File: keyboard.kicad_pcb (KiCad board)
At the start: 2 copper layers, 138.6 x 152.9 mm, 53 parts, among them SW1 SW_PUSH, U1 ATMEGA32U4, X1 XTAL_GND

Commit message: AHHHHHHHHHHHHHHHHHH
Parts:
- removed C1, C2, C3, C4, C5, C6, C7: 22pF, Capacitor_SMD:C_0805_2012Metric_Pad1.15x1.40mm_HandSolder
- removed D_SPACE: D, keyboard_parts:D_SOD123_axial
- removed K_SPACE: KEYSW, MX_Alps_Hybrid:MX-1U-NoLED
- removed R1, R2: 10k, Resistor_SMD:R_0805_2012Metric_Pad1.15x1.40mm_HandSolder
- removed R3, R4: 22, Resistor_SMD:R_0805_2012Metric_Pad1.15x1.40mm_HandSolder
- removed SW1: SW_PUSH, Button_Switch_SMD:SW_SPST_TL3342
- removed USB1: Molex-0548190589, keyboard_parts:Molex-0548190589-Assembly
- removed X1: XTAL_GND, Crystal:Crystal_SMD_5032-4Pin_5.0x3.2mm
- added D_SPACE19: D, keyboard_parts:D_SOD123_axial, F.Cu at (292.9, 131.0)
- added K_SPACE19: KEYSW, MX_Alps_Hybrid:MX-1U-NoLED, F.Cu at (292.9, 126.2)
- U1: value ATMEGA32U4 -> Elite-C-castellated-24pin; footprint Package_QFP:TQFP-44_10x10mm_P0.8mm -> Keebio-Parts:Elite-C-castellated-24pin
- moved K_SPACE10 241.9 mm to (331.0, 173.8)
- moved K_SPACE6 241.9 mm to (254.8, 173.8)
- moved K_SPACE18 239.7 mm to (292.9, 245.3)
- moved K_SPACE4 239.7 mm to (221.5, 150.0)
- moved K_SPACE2 239.7 mm to (254.8, 131.0)
- moved K_SPACE9 239.7 mm to (311.9, 169.1)
- moved K_SPACE1 239.7 mm to (235.7, 131.0)
- moved K_SPACE11 239.7 mm to (221.5, 188.1)
- moved K_SPACE12 239.7 mm to (292.9, 188.1)
- moved K_SPACE13 239.7 mm to (235.7, 207.2)
- moved K_SPACE15 239.7 mm to (273.8, 207.2)
- moved K_SPACE16 239.7 mm to (292.9, 207.2)
- moved K_SPACE17 239.7 mm to (292.9, 226.2)
- moved K_SPACE3 239.7 mm to (273.8, 131.0)
- moved K_SPACE5 239.7 mm to (221.5, 169.1)
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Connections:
- D_SPACE1 pad 1: /row1 -> row0
- D_SPACE10 pad 1: /row3 -> row1
- D_SPACE11 pad 1: /row4 -> row2
- D_SPACE12 pad 1: /row4 -> row2
- D_SPACE13 pad 1: /row5 -> row2
- D_SPACE14 pad 1: /row5 -> row2
- D_SPACE15 pad 1: /row5 -> row2
- D_SPACE16 pad 1: /row5 -> row3
- D_SPACE17 pad 1: /row6 -> row4
- D_SPACE18 pad 1: /row7 -> row5
- D_SPACE2 pad 1: /row1 -> row0
- D_SPACE3 pad 1: /row1 -> row0
- D_SPACE4 pad 1: /row2 -> row0
- D_SPACE5 pad 1: /row3 -> row1
- D_SPACE6 pad 1: /row3 -> row1
- D_SPACE7 pad 1: /row3 -> row1
- D_SPACE8 pad 1: /row3 -> row1
- D_SPACE9 pad 1: /row3 -> row1
- K_SPACE1 pad 1: /col1 -> col1
- K_SPACE10 pad 1: /col6 -> col6
- K_SPACE11 pad 1: /col0 -> col0
- K_SPACE12 pad 1: /col4 -> col4
- K_SPACE13 pad 1: /col1 -> col1
- K_SPACE14 pad 1: /col2 -> col2
- K_SPACE15 pad 1: /col3 -> col3
- K_SPACE16 pad 1: /col4 -> col4
- K_SPACE17 pad 1: /col4 -> col4
- K_SPACE18 pad 1: /col4 -> col4
- K_SPACE2 pad 1: /col2 -> col2
- K_SPACE3 pad 1: /col3 -> col3
- K_SPACE4 pad 1: /col0 -> col0
- K_SPACE5 pad 1: /col0 -> col0
- K_SPACE6 pad 1: /col2 -> col2
- K_SPACE7 pad 1: /col3 -> col3
- K_SPACE8 pad 1: /col4 -> col4
- K_SPACE9 pad 1: /col5 -> col5
- U1 pad 1: Net-(U1-Pad1) -> unconnected-(U1-Pad1)
- U1 pad 10: /row2 -> row5
- U1 pad 11: /row3 -> unconnected-(U1-Pad11)
- U1 pad 12: /row7 -> unconnected-(U1-Pad12)
- U1 pad 13: Net-(R1-Pad1) -> col0
- U1 pad 14: VCC -> col1
- U1 pad 15: GND -> col2
- U1 pad 16: Net-(C1-Pad1) -> col3
- U1 pad 17: Net-(C2-Pad1) -> col4
- U1 pad 18: /col2 -> col5
- U1 pad 19: /col3 -> col6
- U1 pad 2: VCC -> unconnected-(U1-Pad2)
- U1 pad 20: /col4 -> unconnected-(U1-Pad20)
- U1 pad 21: /col5 -> unconnected-(U1-Pad21)
- U1 pad 22: Net-(U1-Pad22) -> unconnected-(U1-Pad22)
- U1 pad 23: GND -> unconnected-(U1-Pad23)
- U1 pad 24: VCC -> unconnected-(U1-Pad24)
- U1 pad 3: Net-(R3-Pad1) -> unconnected-(U1-Pad3)
- U1 pad 4: Net-(R4-Pad1) -> unconnected-(U1-Pad4)
- U1 pad 5: GND -> row0
- U1 pad 6: Net-(C3-Pad1) -> row1
- U1 pad 7: Net-(U1-Pad7) -> row2
- U1 pad 8: /row0 -> row3
- U1 pad 9: /row1 -> row4
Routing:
- net row1: track 0.00 -> 194.1 mm, vias 0 -> 1
- net row2: track 0.00 -> 188.3 mm, vias 0 -> 2
- net row0: track 0.00 -> 145.7 mm, vias 0 -> 2
- net row5: track 0.00 -> 142.5 mm, vias 0 -> 1
- net row4: track 0.00 -> 122.9 mm, vias 0 -> 1
- net col6: track 0.00 -> 108.7 mm
- net col2: track 0.00 -> 102.3 mm
- net col0: track 0.00 -> 102.1 mm
- net col3: track 0.00 -> 91.9 mm
- net col5: track 0.00 -> 88.3 mm
- net col1: track 0.00 -> 39.8 mm
- net col4: track 0.00 -> 31.8 mm, vias 0 -> 1
- net Net-(D_SPACE14-Pad2): track 0.00 -> 9.84 mm
- net Net-(D_SPACE2-Pad2): track 0.00 -> 9.84 mm
- net Net-(D_SPACE13-Pad2): track 0.00 -> 9.84 mm
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- removed copper zone on B.Cu, net GND
- removed copper zone on F.Cu, net VCC
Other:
- board size 138.6 x 152.9 mm -> 131 x 166.7 mm
- net class Default removed

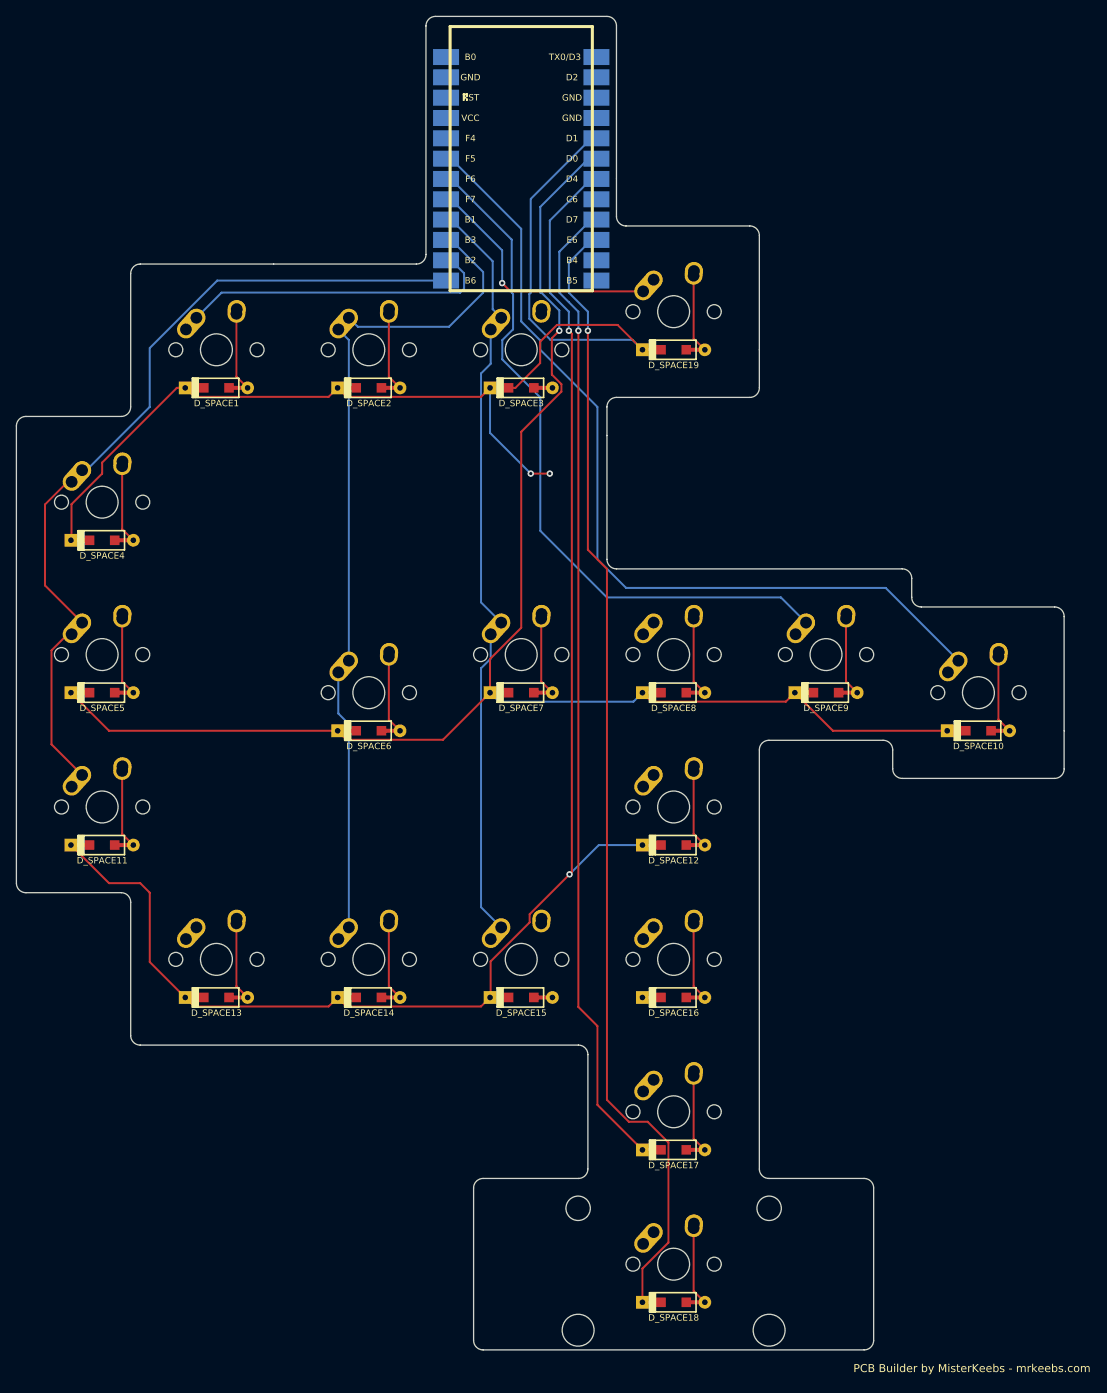
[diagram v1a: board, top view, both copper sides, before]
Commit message: RP2040 rework
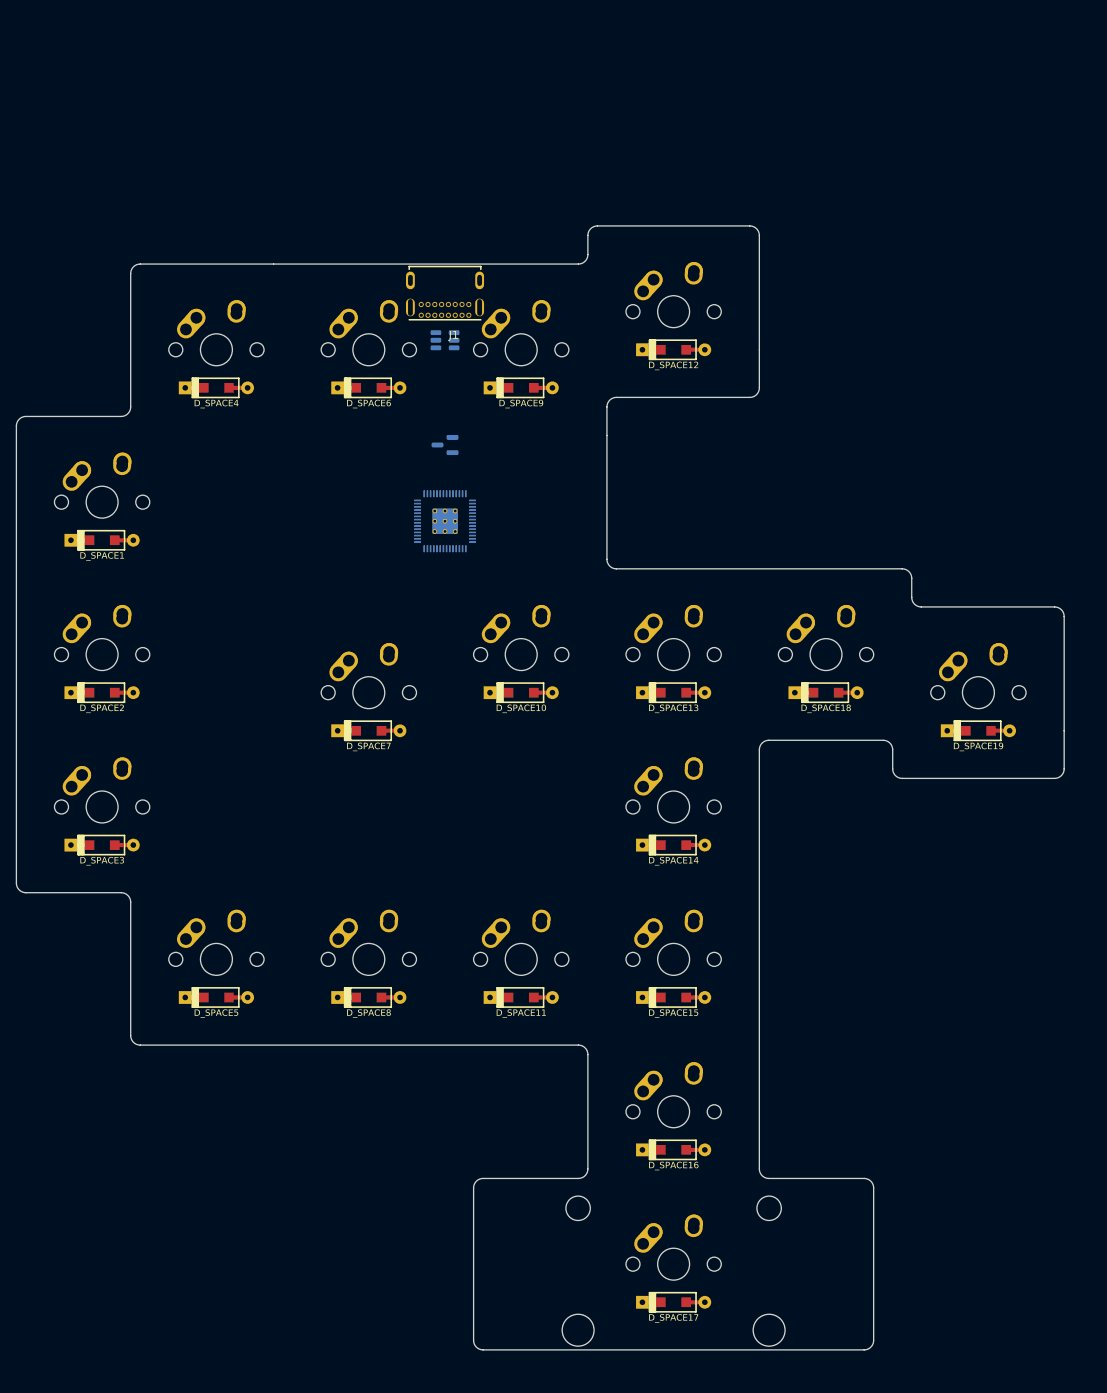
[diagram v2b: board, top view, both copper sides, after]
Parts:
- added J1: USB4085-GF-A_REVA4, LordsBoard:GCT_USB4085-GF-A_REVA4, F.Cu at (264.3, 122.6)
- added U2: SRV05-4, Package_TO_SOT_SMD:SOT-23-6, B.Cu at (264.3, 129.8)
- added U3: RP2040, MCU_RaspberryPi_and_Boards:RP2040-QFN-56, B.Cu at (264.3, 152.4)
- U1: value Elite-C-castellated-24pin -> XC6206P332MR; footprint Keebio-Parts:Elite-C-castellated-24pin -> Package_TO_SOT_SMD:SOT-23
- moved U1 35.8 mm to (264.3, 142.9), turned to 180 degrees
- renumbered D_SPACE4 to D_SPACE1, D_SPACE7 to D_SPACE10, D_SPACE15 to D_SPACE11, D_SPACE19 to D_SPACE12, D_SPACE8 to D_SPACE13, D_SPACE12 to D_SPACE14, D_SPACE16 to D_SPACE15, D_SPACE17 to D_SPACE16, D_SPACE18 to D_SPACE17, D_SPACE9 to D_SPACE18, D_SPACE10 to D_SPACE19, D_SPACE5 to D_SPACE2, D_SPACE11 to D_SPACE3, D_SPACE1 to D_SPACE4, D_SPACE13 to D_SPACE5, D_SPACE2 to D_SPACE6, D_SPACE6 to D_SPACE7, D_SPACE14 to D_SPACE8, D_SPACE3 to D_SPACE9, K_SPACE4 to K_SPACE1, K_SPACE7 to K_SPACE10, K_SPACE15 to K_SPACE11, K_SPACE19 to K_SPACE12, K_SPACE8 to K_SPACE13, K_SPACE12 to K_SPACE14, K_SPACE16 to K_SPACE15, K_SPACE17 to K_SPACE16, K_SPACE18 to K_SPACE17, K_SPACE9 to K_SPACE18, K_SPACE10 to K_SPACE19, K_SPACE5 to K_SPACE2, K_SPACE11 to K_SPACE3, K_SPACE1 to K_SPACE4, K_SPACE13 to K_SPACE5, K_SPACE2 to K_SPACE6, K_SPACE6 to K_SPACE7, K_SPACE14 to K_SPACE8, K_SPACE3 to K_SPACE9
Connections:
- U1 pad 1: unconnected-(U1-Pad1) -> GND
- U1 pad 2: unconnected-(U1-Pad2) -> +3V3
- U1 pad 3: unconnected-(U1-Pad3) -> +5V
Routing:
- net row1: track 194.1 -> 0.00 mm, vias 1 -> 0
- net row2: track 188.3 -> 0.00 mm, vias 2 -> 0
- net row0: track 145.7 -> 0.00 mm, vias 2 -> 0
- net row5: track 142.5 -> 0.00 mm, vias 1 -> 0
- net row4: track 122.9 -> 0.00 mm, vias 1 -> 0
- net col6: track 108.7 -> 0.00 mm
- net col2: track 102.3 -> 0.00 mm
- net col0: track 102.1 -> 0.00 mm
- net col3: track 91.9 -> 0.00 mm
- net col5: track 88.3 -> 0.00 mm
- net col1: track 39.8 -> 0.00 mm
- net col4: track 31.8 -> 0.00 mm, vias 1 -> 0
- net Net-(D_SPACE8-Pad2): track 9.84 -> 0.00 mm
- net Net-(D_SPACE6-Pad2): track 9.84 -> 0.00 mm
- net Net-(D_SPACE5-Pad2): track 9.84 -> 0.00 mm
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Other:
- board size 131 x 166.7 mm -> 131 x 140.5 mm
- board text removed: "PCB Builder by MisterKeebs - mrkeebs.com"

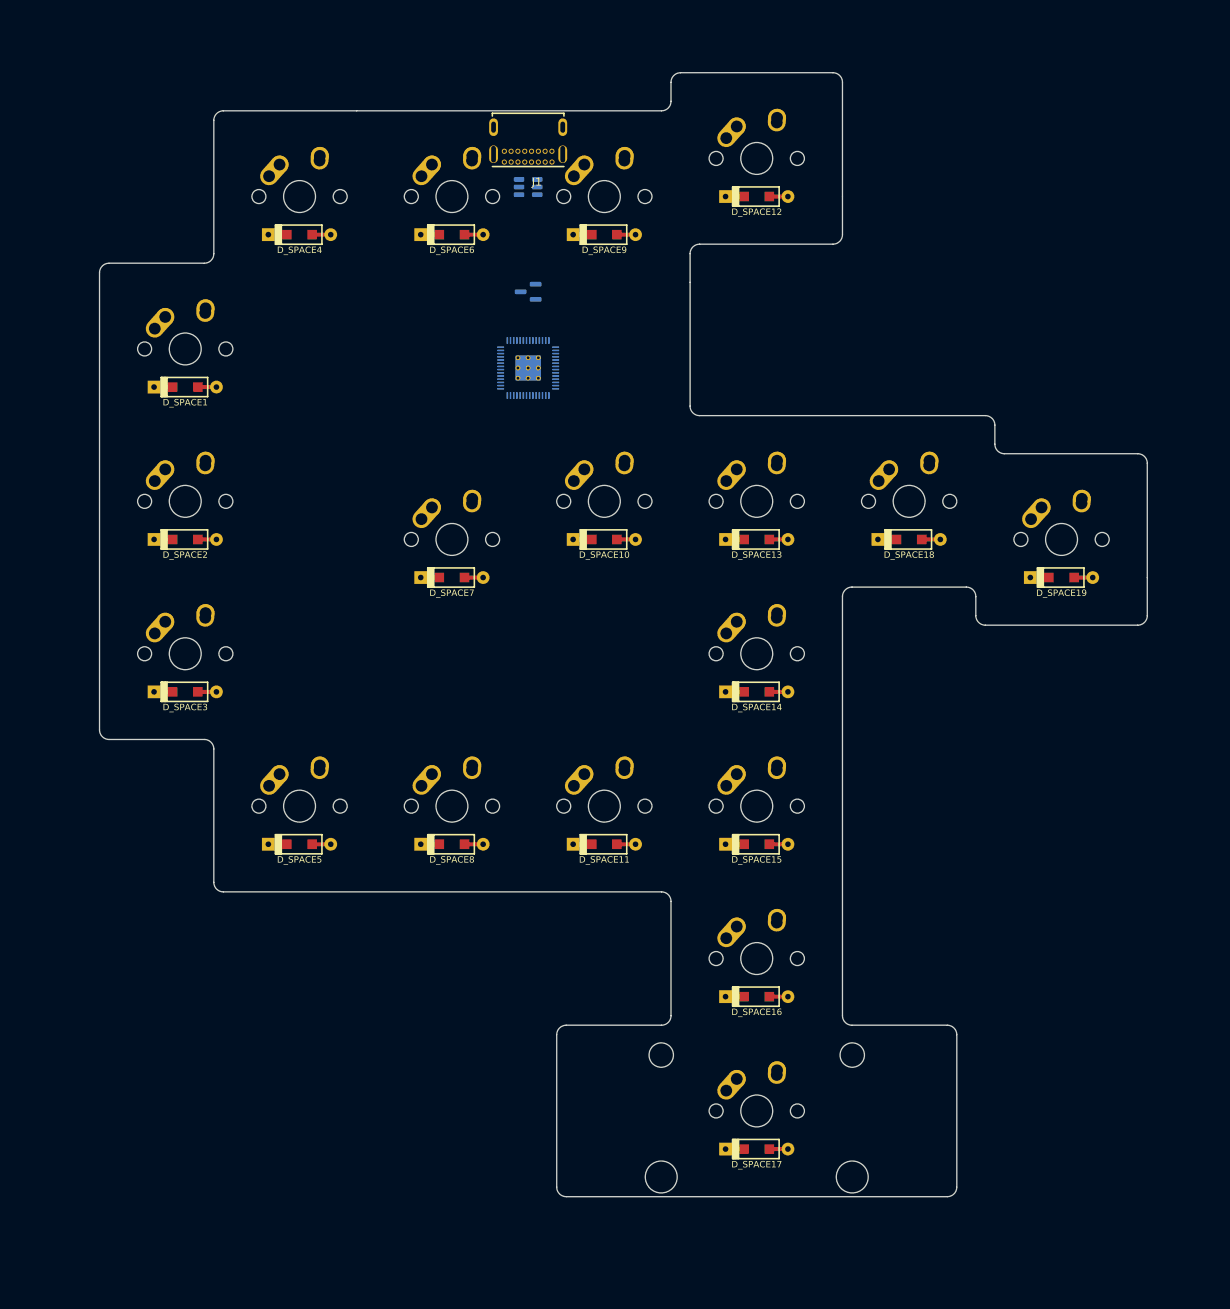
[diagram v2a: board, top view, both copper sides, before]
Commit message: Changes to keyboard schematic--added QSPI flash.  TODO: add decoupling caps.
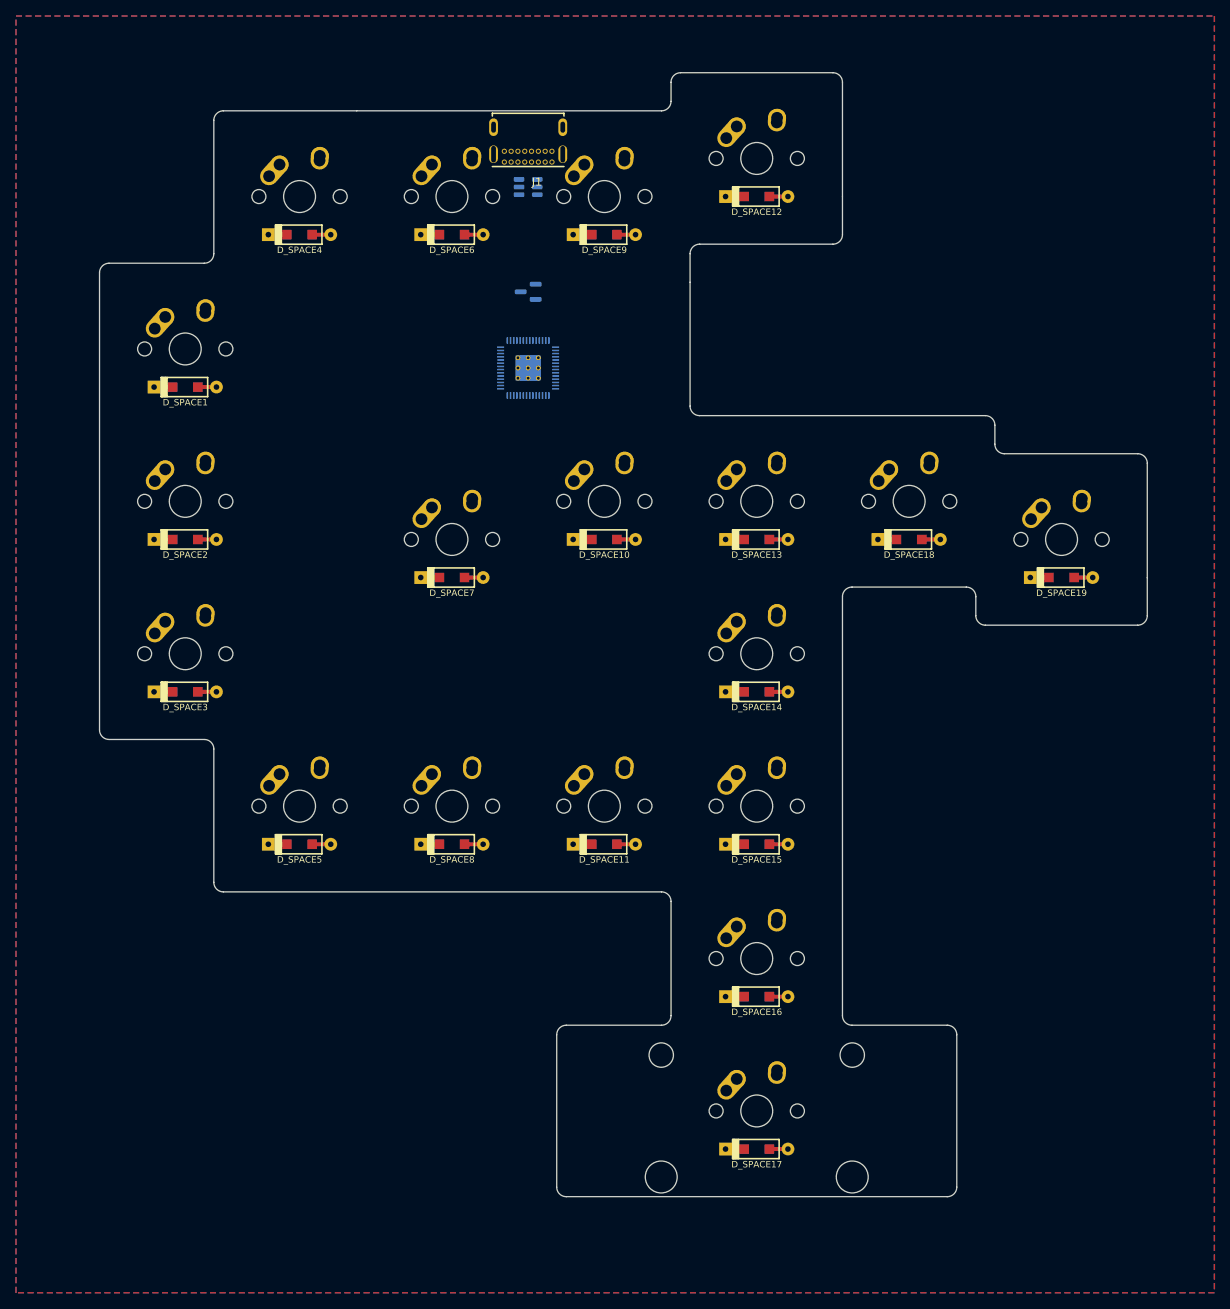
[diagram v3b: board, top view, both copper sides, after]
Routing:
- added copper zone on B.Cu, net GND
- added copper zone on F.Cu, net GND
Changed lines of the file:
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@@
   (gr_line (start 210.740625 140.49375) (end 210.740625 197.64375) (layer "Edge.Cuts") (width 0.1))
   (gr_line (start 283.36875 115.490625) (end 302.41875 115.490625) (layer "Edge.Cuts") (width 0.1))
+  (segment (start 263.89375 126.659375) (end 263.89375 126.80625) (width 0.2) (layer "B.Cu") (net 34))
+  (zone (net 36) (net_name "GND") (layers F&B.Cu) (hatch edge 0.508)
+    (connect_pads (clearance 0.508))
+    (min_thickness 0.254) (filled_areas_thickness no)
+    (fill yes (thermal_gap 0.508) (thermal_bridge_width 0.508))
+    (polygon
+      (pts
+        (xy 200.3 108.4)
+        (xy 350.1 108.4)
+        (xy 350.1 268)
+        (xy 200.3 268)
+      )
+    )
+  )
 )
